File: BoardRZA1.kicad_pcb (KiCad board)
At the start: 4 copper layers, 100 x 80 mm, 109 parts, among them CON1 USB-MINI-B, CON2 USB-MINI-B, CON3 con-microSD, P1 CONN_5X2, U1 RZ-A1L, U2 OSC_4PIN, U3 OSC_4PIN, U4 N25QXXX, U5 AS4C16M16S, X1 32.768k

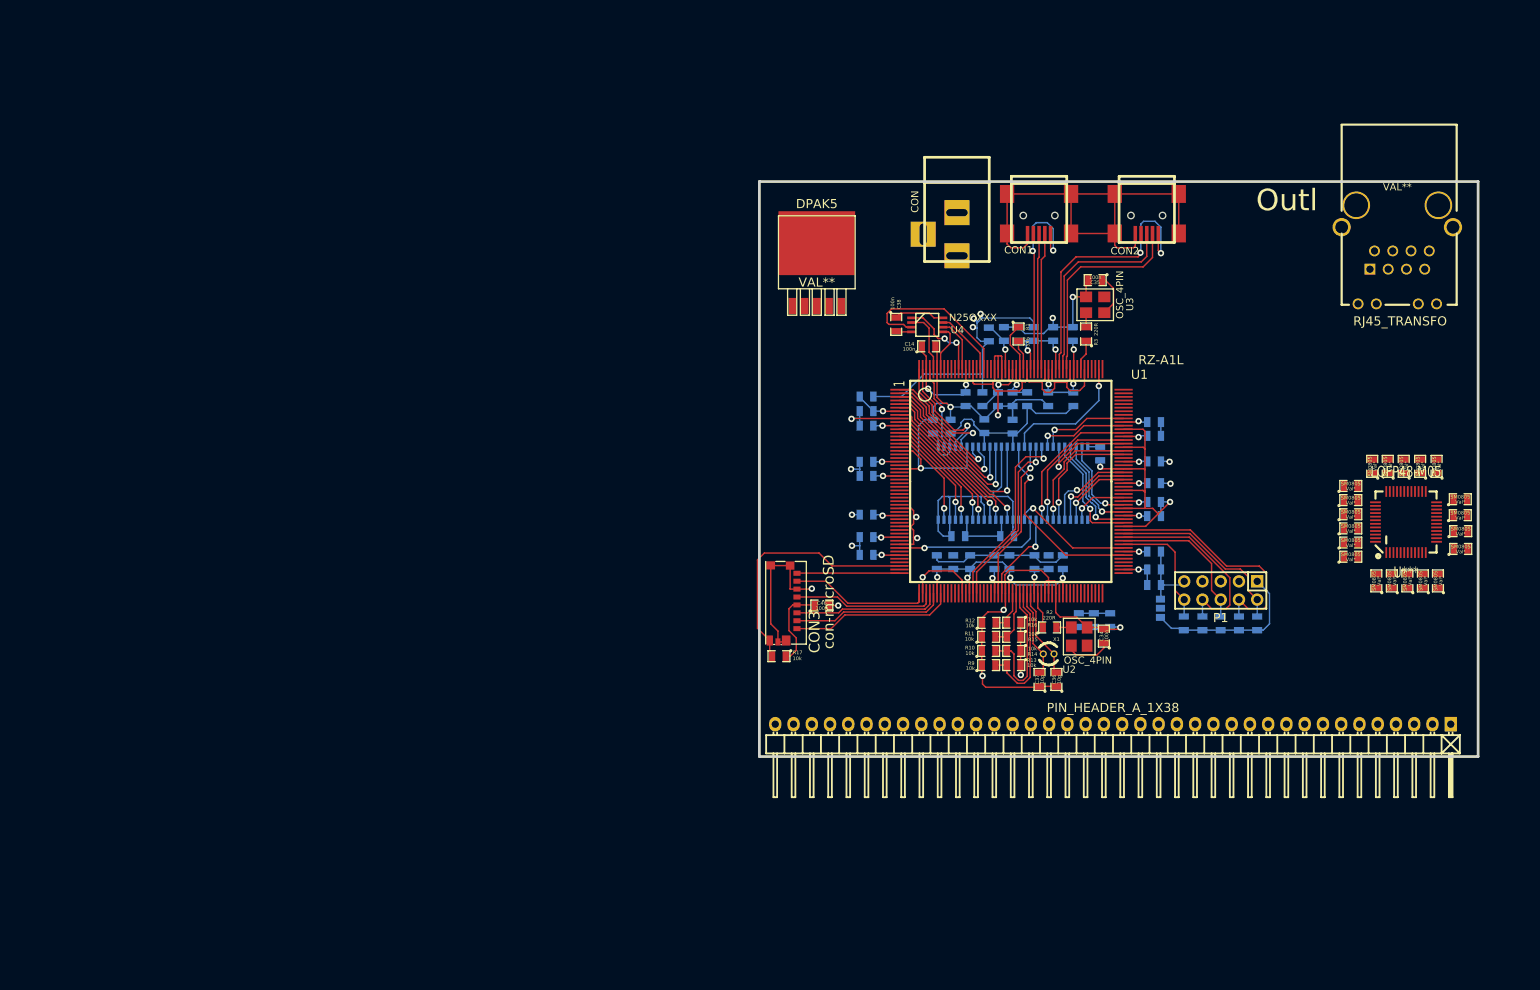
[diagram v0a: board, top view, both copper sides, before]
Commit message: Ruteo de power. Reogranizado de la plaqueta y planos de masa
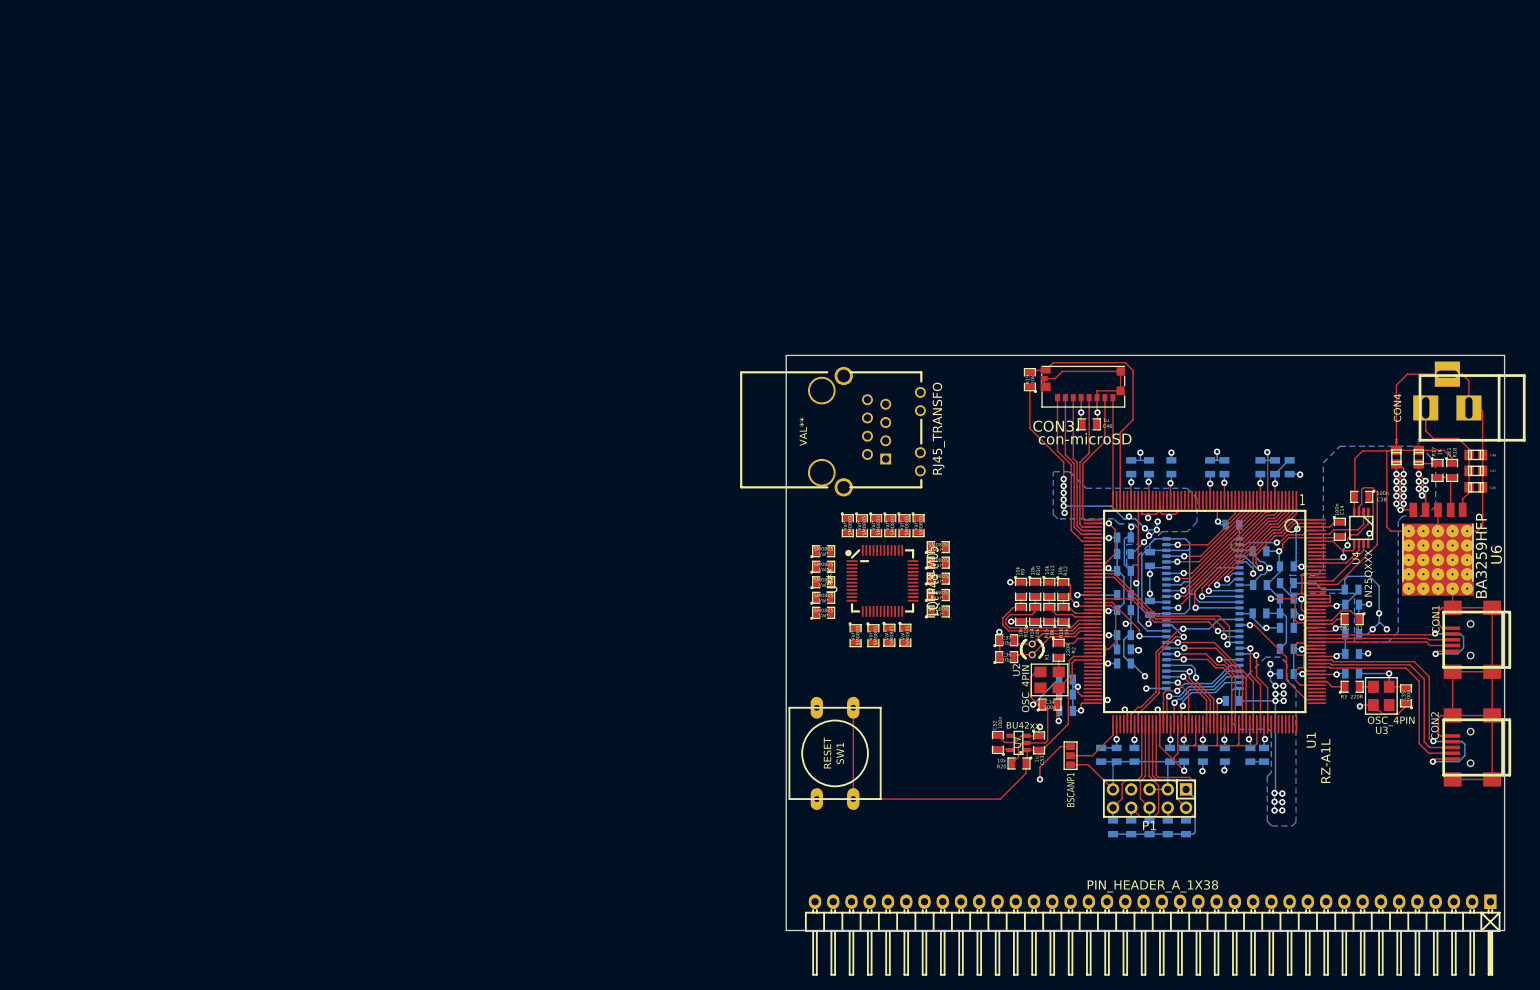
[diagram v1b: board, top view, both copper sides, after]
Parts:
- removed CON: BARREL_JACK, Connect:BARREL_JACK
- removed DPAK5: VAL**, SMD_Packages:DPAK5
- removed Outl: EuroBoard_halb_Type-I_100mmX80mm, EuroBoard_Outline:EuroBoard_halb_Type-I_100mmX80mm
- added C47: 1u, Capacitors_SMD:c_0805, F.Cu at (221.9, 77.5)
- added C48: 1u, Capacitors_SMD:c_0805, F.Cu at (221.9, 79.8)
- added C49: 1u, Capacitors_SMD:c_0805, F.Cu at (221.9, 75.3)
- added C50: 1u, Capacitors_SMD:c_0805, F.Cu at (214.0, 75.6)
- added C51: 100n, Capacitors_SMD:c_0805, F.Cu at (210.9, 75.6)
- added C52: 100n, SMD_Packages:SM0805, F.Cu at (155.4, 115.3)
- added C53: 1u, SMD_Packages:SM0805, F.Cu at (161.2, 115.4)
- added CON4: BARREL_JACK, Connect:BARREL_JACK, F.Cu at (221.2, 68.8)
- added R18: 2K1, SMD_Packages:SM0805, F.Cu at (218.6, 77.5)
- added R19: 10k, SMD_Packages:SM0805, F.Cu at (159.9, 64.8)
- added R20: 10k, SMD_Packages:SM0805, F.Cu at (158.4, 118.2)
- added SW1: RESET, Discret:SW_PUSH-12mm, F.Cu at (132.8, 116.8)
- added U6: BA3259HFP, Rohm:Rohm-HRP5, F.Cu at (216.7, 84.9)
- added U7: BU42xx, Rohm:SSOP-5, F.Cu at (158.3, 115.4)
- BSCANP1: moved to F.Cu
- C46: value 100n -> 1u
- R17: value 10k -> 1K
- moved R17 95.2 mm to (216.6, 77.5), turned to 270 degrees
- moved CON2 87.8 mm to (222.1, 116.0), turned to 180 degrees
- moved SM0805 85.6 mm to (131.2, 97.3), turned to 0 degrees
- moved CON1 85.4 mm to (222.1, 101.0), turned to 180 degrees
- moved SM0805 85.1 mm to (135.6, 100.5), turned to 270 degrees
- moved SM0805 83.4 mm to (131.2, 95.2), turned to 0 degrees
- moved SM0805 83.0 mm to (138.1, 100.5), turned to 270 degrees
- moved SM0805 81.2 mm to (131.2, 93.0), turned to 0 degrees
- moved SM0805 81.2 mm to (140.3, 100.4), turned to 270 degrees
- moved SM0805 79.5 mm to (142.6, 100.4), turned to 270 degrees
- moved SM0805 79.1 mm to (131.2, 90.9), turned to 0 degrees
- moved SM0805 77.0 mm to (131.2, 88.7), turned to 0 degrees
- moved LQFP48-M05 73.3 mm to (139.4, 92.8), turned to 270 degrees
- moved RJ45_TRANSFO 72.4 mm to (139.8, 75.9), turned to 270 degrees
- moved C35 72.2 mm to (212.2, 108.8), turned to 90 degrees
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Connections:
- R17 pad 1: +3.3V -> +1.2V
- R17 pad 2: /SD_CD_1 -> Net-(R17-Pad2)
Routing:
- net +3.3V: track 107.2 -> 230.0 mm, vias 1 -> 47
- net VSS: track 449.5 -> 553.5 mm, vias 21 -> 31
- net /VCC: track 27.4 -> 128.8 mm
- net /PVCC: track 81.8 -> 175.6 mm
- net /RESET: track 0.00 -> 60.5 mm
- net Net-(C47-Pad1): track 0.00 -> 19.1 mm
- net /JTAG_TMS: track 25.9 -> 14.8 mm
- net +1.2V: track 39.1 -> 49.2 mm, vias 3 -> 12
- net /JTAG_TCK: track 33.8 -> 24.0 mm
- net /JTAG_TDI: track 27.8 -> 19.2 mm
- net Net-(BSCANP1-Pad2): track 0.00 -> 8.60 mm
- net /AVcc: track 4.38 -> 12.0 mm, vias 0 -> 2
- net /JTAG_TDO: track 21.4 -> 14.2 mm
- net Net-(R17-Pad2): track 0.00 -> 6.65 mm
- net /PLLVCC: track 5.37 -> 7.62 mm
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- added copper zone on B.Cu, net +1.2V
- added copper zone on In1.Cu, net +1.2V
- added copper zone on B.Cu, net +3.3V
- added copper zone on In1.Cu, net +3.3V
- added copper zone on In1.Cu, net /PVCC
- added copper zone on In1.Cu, net /VCC
- added copper zone on In2.Cu, net VSS
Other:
- board size 100 x 80 mm -> 99.9 x 80 mm

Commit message: Actualizado preview 3d
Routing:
- net VSS: track 553.5 -> 554.7 mm, vias 31 -> 32

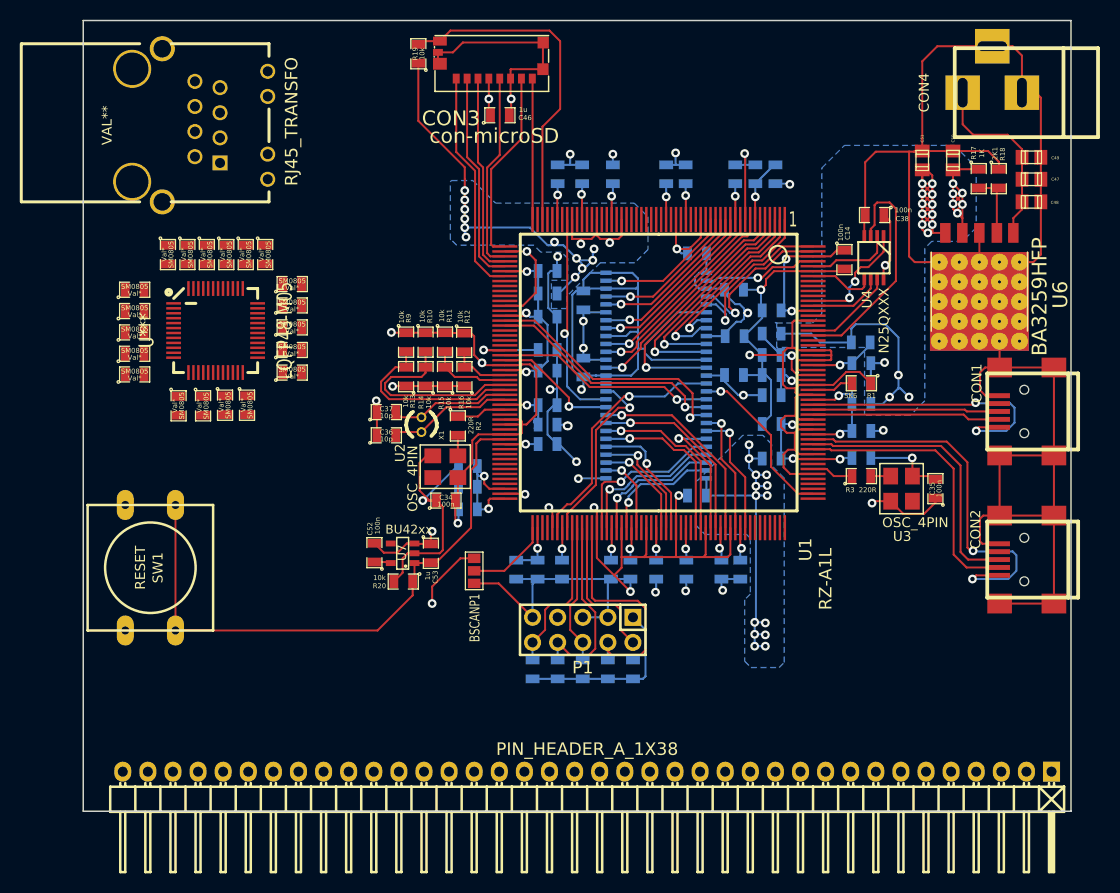
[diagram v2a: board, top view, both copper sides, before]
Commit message: Add ETH Add reset system Correct clock footprint Finish main routing and power/gnd planes
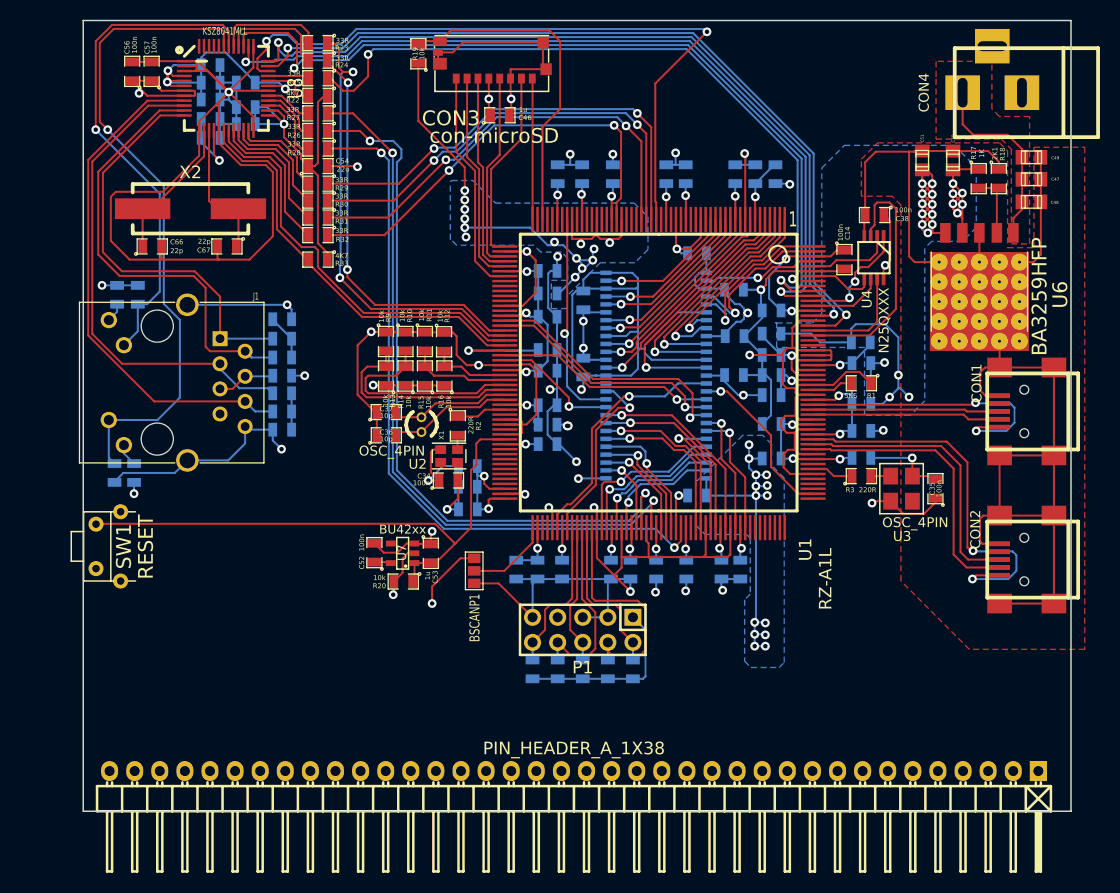
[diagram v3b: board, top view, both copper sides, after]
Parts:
- removed LQFP48-M05: U***, smd_qfp:LQFP48-M05
- removed RJ45_TRANSFO: VAL**, Connect:RJ45_TRANSFO
- removed SM0805 (x20): Val*, SMD_Packages:SM0805
- added C54: 22u, SMD_Packages:SM0805, F.Cu at (149.7, 76.2)
- added C55: 100n, SMD_Packages:SM0805, B.Cu at (142.4, 71.9)
- added C56: 100n, SMD_Packages:SM0805, F.Cu at (130.9, 66.6)
- added C57: 100n, SMD_Packages:SM0805, F.Cu at (132.9, 66.6)
- added C58: 100p, SMD_Packages:SM0805, B.Cu at (138.9, 71.4)
- added C59: 100n, SMD_Packages:SM0805, B.Cu at (142.4, 70.2)
- added C60: 100n, SMD_Packages:SM0805, B.Cu at (138.9, 66.0)
- added C61: 100n, SMD_Packages:SM0805, B.Cu at (138.9, 67.8)
- added C62: 100n, SMD_Packages:SM0805, B.Cu at (142.4, 67.8)
- added C63: 22u, SMD_Packages:SM0805, B.Cu at (138.9, 69.5)
- added C64: 100n, SMD_Packages:SM0805, B.Cu at (146.1, 91.7)
- added C65: 100n, SMD_Packages:SM0805, B.Cu at (146.1, 102.9)
- added C66: 22p, SMD_Packages:SM0805, F.Cu at (133.0, 84.3)
- added C67: 22p, SMD_Packages:SM0805, F.Cu at (140.5, 84.3)
- added J1: HR911105A, RJ45:RJ45_Pulse_J403-A, F.Cu at (133.5, 98.1)
- added L10: BLM18PG600, SMD_Packages:SM0805, B.Cu at (146.1, 97.4)
- added R21: 6.49k, SMD_Packages:SM0805, B.Cu at (138.9, 73.3)
- added R22: 4K7, SMD_Packages:SM0805, F.Cu at (149.7, 69.1)
- added R23: 33R, SMD_Packages:SM0805, F.Cu at (149.7, 63.8)
- added R24: 33R, SMD_Packages:SM0805, F.Cu at (149.7, 65.5)
- added R25: 33R, SMD_Packages:SM0805, F.Cu at (149.7, 67.3)
- added R26: 33R, SMD_Packages:SM0805, F.Cu at (149.7, 72.6)
- added R27: 33R, SMD_Packages:SM0805, F.Cu at (149.7, 70.9)
- added R28: 33R, SMD_Packages:SM0805, F.Cu at (149.7, 74.4)
- added R29: 33R, SMD_Packages:SM0805, F.Cu at (149.7, 78.0)
- added R30: 33R, SMD_Packages:SM0805, F.Cu at (149.7, 79.7)
- added R31: 33R, SMD_Packages:SM0805, F.Cu at (149.7, 81.4)
- added R32: 33R, SMD_Packages:SM0805, F.Cu at (149.7, 83.2)
- added R33: 4K7, SMD_Packages:SM0805, F.Cu at (149.7, 85.7)
- added R34: 4K7, SMD_Packages:SM0805, B.Cu at (131.5, 89.2)
- added R35: 4K7, SMD_Packages:SM0805, B.Cu at (129.2, 107.3)
- added R36: 220R, SMD_Packages:SM0805, B.Cu at (129.4, 89.2)
- added R37: 220R, SMD_Packages:SM0805, B.Cu at (131.1, 107.3)
- added R38: 49.9, SMD_Packages:SM0805, B.Cu at (146.1, 93.7)
- added R39: 49.9, SMD_Packages:SM0805, B.Cu at (146.1, 95.6)
- added R40: 49.9, SMD_Packages:SM0805, B.Cu at (146.1, 99.2)
- added R41: 49.9, SMD_Packages:SM0805, B.Cu at (146.1, 101.0)
- added U8: KSZ8041MLL, smd_qfp:LQFP48-M05, F.Cu at (140.5, 68.3)
- added X2: 20MHz, Crystals:Crystal_HC49-SD_SMD, F.Cu at (136.8, 80.5)
- SW1: footprint Discret:SW_PUSH-12mm -> PushButton:RigthAnglePush
- U2: footprint OSC_4PIN:OSC_4PIN -> OSC_4PIN:OSC_2x2p5
- moved SW1 4.77 mm to (128.5, 114.7)
- moved C34 2.05 mm to (162.9, 108.0)
- moved R10 2.03 mm to (158.6, 93.9)
- moved R13 2.03 mm to (156.6, 97.4)
- moved R14 2.03 mm to (158.6, 97.4)
- moved R9 2.03 mm to (156.6, 93.9)
- moved R12 2.03 mm to (162.5, 94.0)
- moved R11 2.03 mm to (160.6, 93.9)
- moved R15 2.03 mm to (160.6, 97.4)
- moved R16 2.03 mm to (162.5, 97.4)
- moved PIN_HEADER_A_1X38 1.34 mm to (175.6, 137.4)
- moved U2 1.14 mm to (163.0, 105.5)
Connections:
- net Net-(U1-Pad201) renamed /TX_TXER
- U1 pad 127: Net-(U1-Pad127) -> /ET_RXCLK
- U1 pad 129: Net-(U1-Pad129) -> /ET_RXER
- U1 pad 135: Net-(U1-Pad135) -> /ET_RXDV
- U1 pad 192: Net-(U1-Pad192) -> /ET_TXD0
- U1 pad 194: Net-(U1-Pad194) -> /ET_TXD1
- U1 pad 198: Net-(U1-Pad198) -> /ET_TXD2
- U1 pad 199: Net-(U1-Pad199) -> /ET_TXD3
- U1 pad 200: Net-(U1-Pad200) -> /ET_TXCLK
- U1 pad 27: Net-(U1-Pad27) -> /ET_TXEN
- U1 pad 28: Net-(U1-Pad28) -> /ET_RXD0
- U1 pad 29: Net-(U1-Pad29) -> /ET_RXD1
- U1 pad 30: Net-(U1-Pad30) -> /ET_RXD2
- U1 pad 35: Net-(U1-Pad35) -> /ET_RXD3
- U1 pad 70: Net-(U1-Pad70) -> /ET_COL
- U1 pad 71: Net-(U1-Pad71) -> /ET_CRS
- U1 pad 72: Net-(U1-Pad72) -> /ET_MDC
- U1 pad 73: Net-(U1-Pad73) -> /ET_MDIO
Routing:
- net VSS: track 554.7 -> 679.3 mm, vias 32 -> 35
- net /ET_TXD3: track 0.00 -> 85.8 mm, vias 0 -> 2
- net /ET_TXD0: track 0.00 -> 83.6 mm, vias 0 -> 2
- net /ET_TXD2: track 0.00 -> 83.3 mm, vias 0 -> 2
- net /ET_TXD1: track 0.00 -> 82.6 mm, vias 0 -> 2
- net /ET_RXCLK: track 0.00 -> 73.7 mm, vias 0 -> 2
- net /ET_RXER: track 0.00 -> 73.1 mm, vias 0 -> 2
- net /ET_RXDV: track 0.00 -> 72.7 mm, vias 0 -> 2
- net /ET_TXEN: track 0.00 -> 71.5 mm, vias 0 -> 2
- net /ET_TXCLK: track 0.00 -> 70.5 mm, vias 0 -> 2
- net /LED1: track 0.00 -> 66.8 mm, vias 0 -> 1
- net Net-(J1-Pad6): track 0.00 -> 51.8 mm
- net /LED0: track 0.00 -> 51.4 mm, vias 0 -> 1
- net Net-(J1-Pad3): track 0.00 -> 50.1 mm
- net +3.3V: track 230.0 -> 277.1 mm, vias 47 -> 53
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- added copper zone on F.Cu, net Net-(C47-Pad1)
- added copper zone on F.Cu, net VSS
